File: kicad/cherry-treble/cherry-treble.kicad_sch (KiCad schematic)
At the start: 103 parts

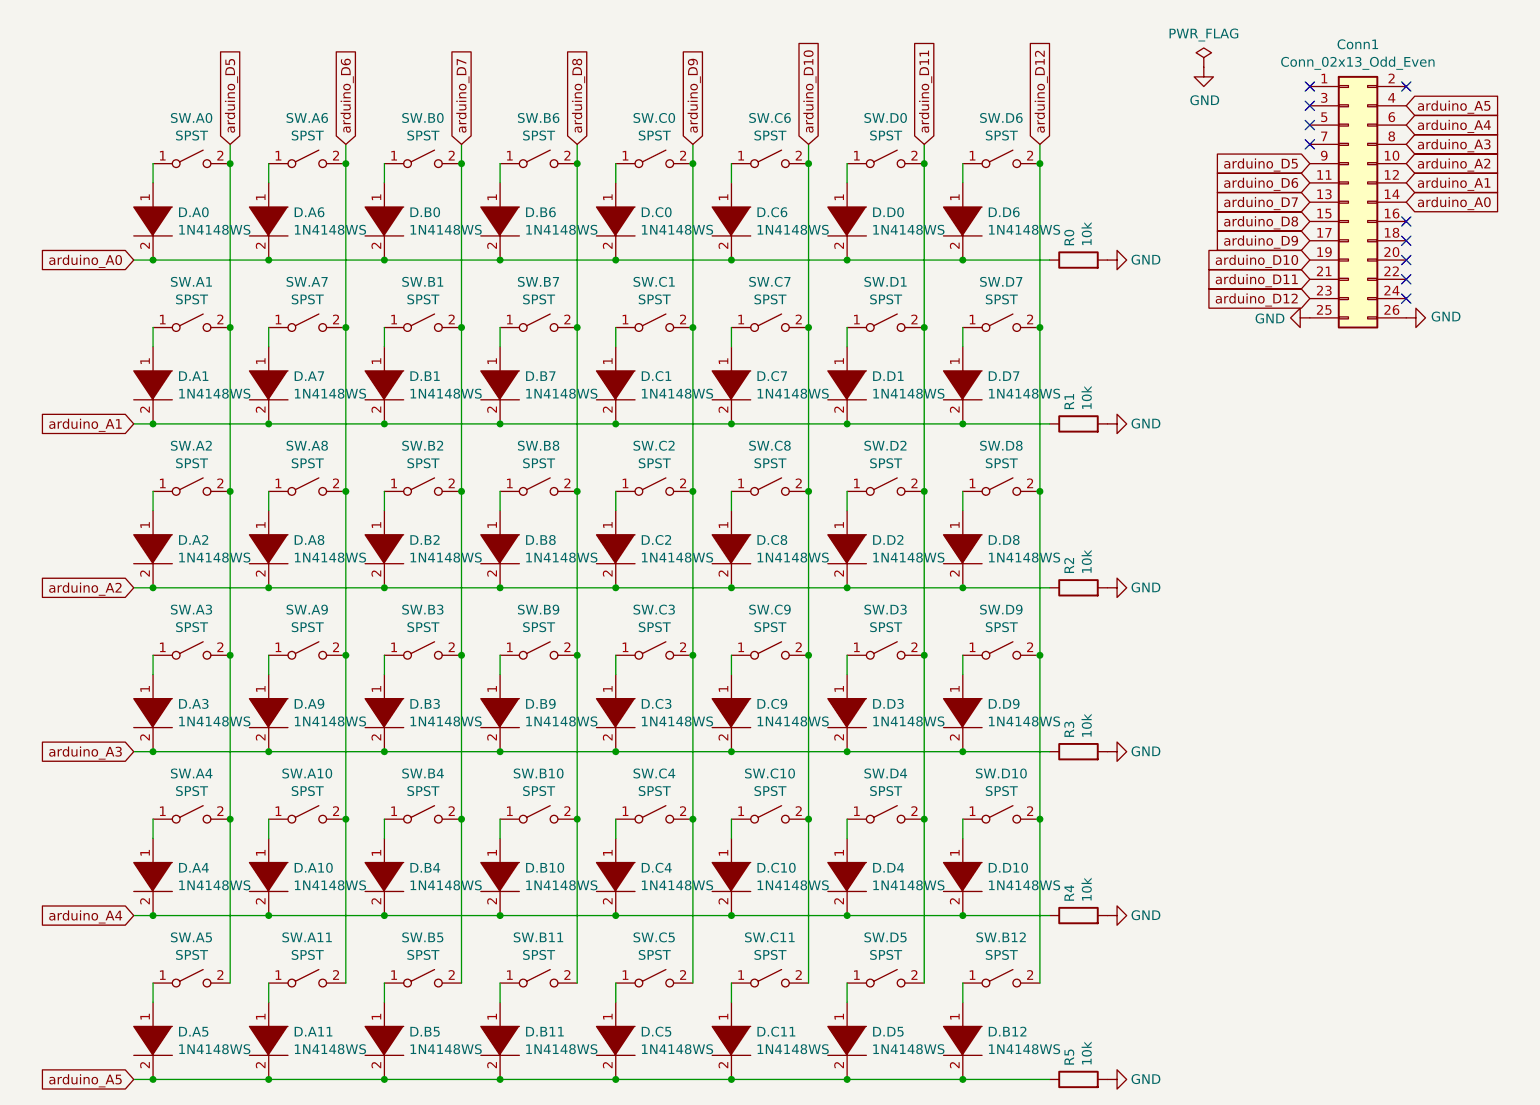
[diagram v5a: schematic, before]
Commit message: Replace diode symbols on cherry treble
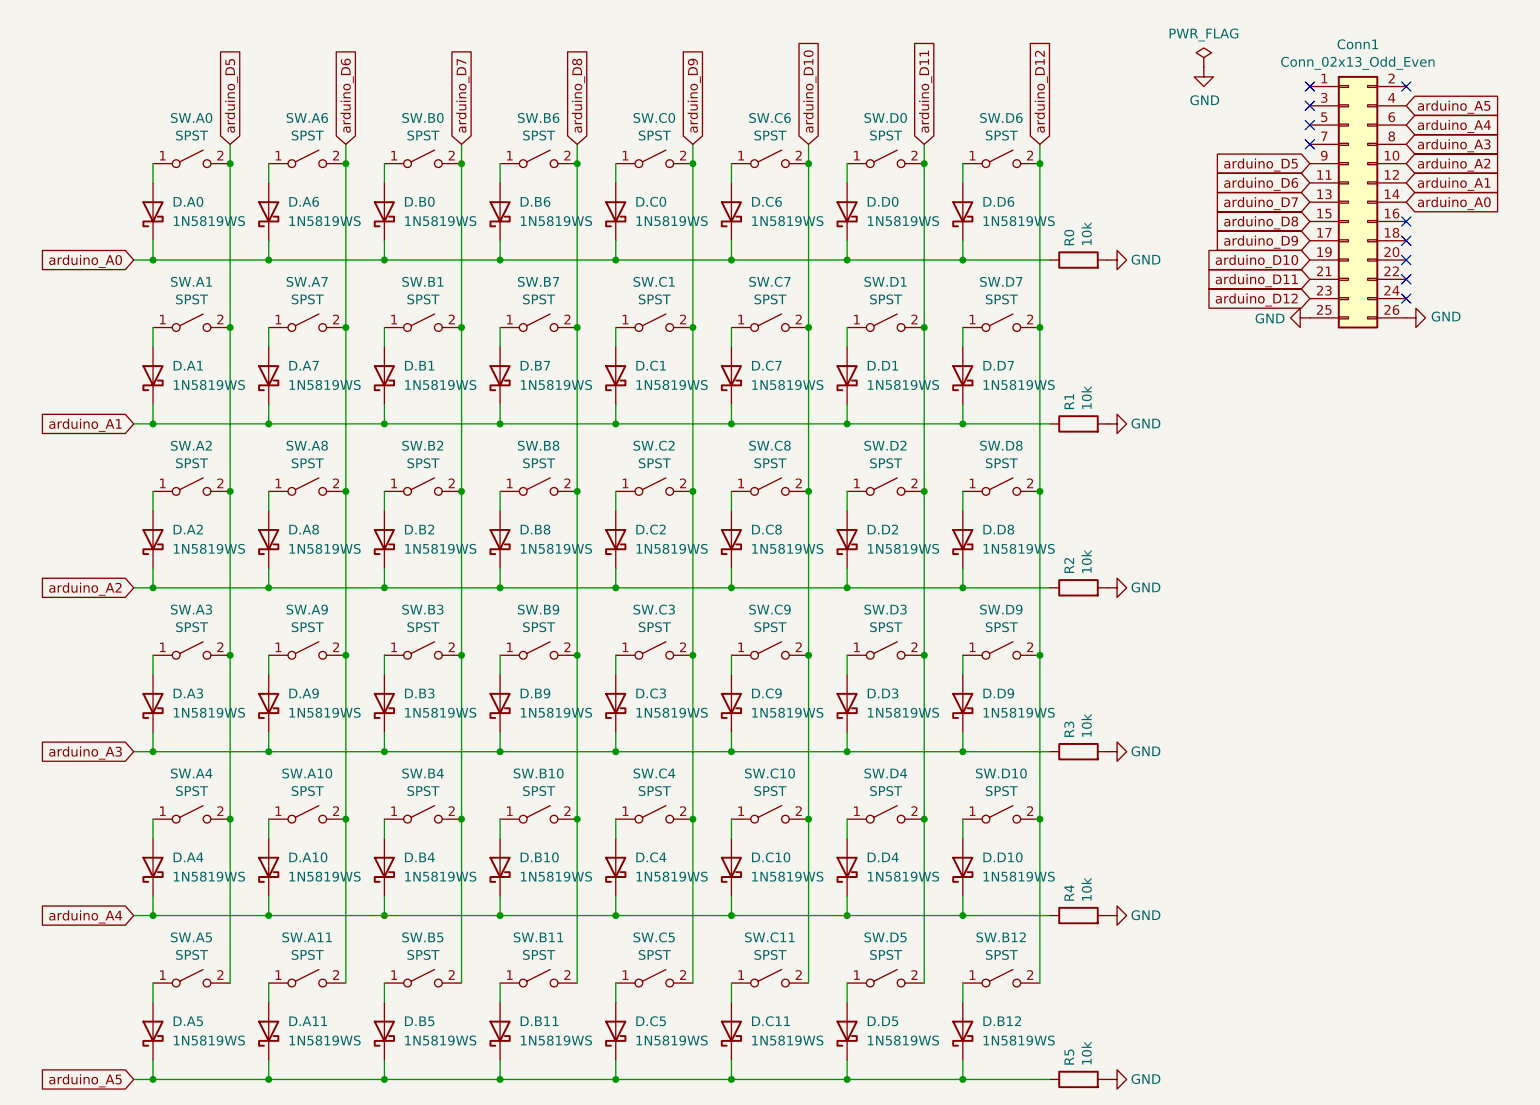
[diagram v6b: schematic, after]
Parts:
- removed D.D6: 1N4148WS, Diode_SMD:D_SOD-323_HandSoldering, symbol pspice:DIODE
- added D.D6: 1N5819WS, Diode_SMD:D_SOD-323_HandSoldering, symbol Diode:1N5819WS
- D.A0, D.A1, D.A10, D.A11, D.A2, D.A3, D.A4, D.A5, D.A6, D.A7, D.A8, D.A9, D.B0, D.B1, D.B10, D.B11, D.B12, D.B2, D.B3, D.B4, D.B5, D.B6, D.B7, D.B8, D.B9, D.C0, D.C1, D.C10, D.C11, D.C2, D.C3, D.C4, D.C5, D.C6, D.C7, D.C8, D.C9, D.D0, D.D1, D.D10, D.D2, D.D3, D.D4, D.D5, D.D7, D.D8, D.D9: value 1N4148WS -> 1N5819WS; symbol pspice:DIODE -> Diode:1N5819WS; LCSC Part # (none) -> C2128
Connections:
- net arduino_A0: now also D.A0.1 (K), D.A6.1 (K), D.B0.1 (K), D.B6.1 (K), D.C0.1 (K), D.C6.1 (K), D.D0.1 (K), D.D6.1 (K); no longer D.A0.2 (A), D.A6.2 (A), D.B0.2 (A), D.B6.2 (A), D.C0.2 (A), D.C6.2 (A), D.D0.2 (A)
- net arduino_A1: now also D.A1.1 (K), D.A7.1 (K), D.B1.1 (K), D.B7.1 (K), D.C1.1 (K), D.C7.1 (K), D.D1.1 (K), D.D7.1 (K); no longer D.A1.2 (A), D.A7.2 (A), D.B1.2 (A), D.B7.2 (A), D.C1.2 (A), D.C7.2 (A), D.D1.2 (A), D.D7.2 (A)
- net arduino_A2: now also D.A2.1 (K), D.A8.1 (K), D.B2.1 (K), D.B8.1 (K), D.C2.1 (K), D.C8.1 (K), D.D2.1 (K), D.D8.1 (K); no longer D.A2.2 (A), D.A8.2 (A), D.B2.2 (A), D.B8.2 (A), D.C2.2 (A), D.C8.2 (A), D.D2.2 (A), D.D8.2 (A)
- net arduino_A3: now also D.A3.1 (K), D.A9.1 (K), D.B3.1 (K), D.B9.1 (K), D.C3.1 (K), D.C9.1 (K), D.D3.1 (K), D.D9.1 (K); no longer D.A3.2 (A), D.A9.2 (A), D.B3.2 (A), D.B9.2 (A), D.C3.2 (A), D.C9.2 (A), D.D3.2 (A), D.D9.2 (A)
- net arduino_A4: now also D.A10.1 (K), D.A4.1 (K), D.B10.1 (K), D.B4.1 (K), D.C10.1 (K), D.C4.1 (K), D.D10.1 (K), D.D4.1 (K); no longer D.A10.2 (A), D.A4.2 (A), D.B10.2 (A), D.B4.2 (A), D.C10.2 (A), D.C4.2 (A), D.D10.2 (A), D.D4.2 (A)
- net arduino_A5: now also D.A11.1 (K), D.A5.1 (K), D.B11.1 (K), D.B12.1 (K), D.B5.1 (K), D.C11.1 (K), D.C5.1 (K), D.D5.1 (K); no longer D.A11.2 (A), D.A5.2 (A), D.B11.2 (A), D.B12.2 (A), D.B5.2 (A), D.C11.2 (A), D.C5.2 (A), D.D5.2 (A)
- net at SW.C4.1 (A): now also D.C4.2 (A); no longer D.C4.1 (K)
- net at SW.C2.1 (A): now also D.C2.2 (A); no longer D.C2.1 (K)
- net at SW.C8.1 (A): now also D.C8.2 (A); no longer D.C8.1 (K)
- net at SW.B4.1 (A): now also D.B4.2 (A); no longer D.B4.1 (K)
- net at SW.D7.1 (A): now also D.D7.2 (A); no longer D.D7.1 (K)
- net at SW.B10.1 (A): now also D.B10.2 (A); no longer D.B10.1 (K)
- net at SW.D6.1 (A): now also D.D6.2 (A)
- net at SW.A6.1 (A): now also D.A6.2 (A); no longer D.A6.1 (K)
- net at SW.A0.1 (A): now also D.A0.2 (A); no longer D.A0.1 (K)
- net at SW.B5.1 (A): now also D.B5.2 (A); no longer D.B5.1 (K)
- net at SW.D1.1 (A): now also D.D1.2 (A); no longer D.D1.1 (K)
- net at SW.D5.1 (A): now also D.D5.2 (A); no longer D.D5.1 (K)
- net at SW.B3.1 (A): now also D.B3.2 (A); no longer D.B3.1 (K)
- net at SW.A5.1 (A): now also D.A5.2 (A); no longer D.A5.1 (K)
- net at SW.A11.1 (A): now also D.A11.2 (A); no longer D.A11.1 (K)
- net at SW.C0.1 (A): now also D.C0.2 (A); no longer D.C0.1 (K)
- net at SW.A4.1 (A): now also D.A4.2 (A); no longer D.A4.1 (K)
- net at SW.D8.1 (A): now also D.D8.2 (A); no longer D.D8.1 (K)
- net at SW.A1.1 (A): now also D.A1.2 (A); no longer D.A1.1 (K)
- net at SW.C11.1 (A): now also D.C11.2 (A); no longer D.C11.1 (K)
- net at SW.C9.1 (A): now also D.C9.2 (A); no longer D.C9.1 (K)
- net at SW.D3.1 (A): now also D.D3.2 (A); no longer D.D3.1 (K)
- net at SW.B2.1 (A): now also D.B2.2 (A); no longer D.B2.1 (K)
- net at SW.A9.1 (A): now also D.A9.2 (A); no longer D.A9.1 (K)
- net at SW.C1.1 (A): now also D.C1.2 (A); no longer D.C1.1 (K)
- net at SW.B9.1 (A): now also D.B9.2 (A); no longer D.B9.1 (K)
- net at SW.B11.1 (A): now also D.B11.2 (A); no longer D.B11.1 (K)
- net at SW.B6.1 (A): now also D.B6.2 (A); no longer D.B6.1 (K)
- net at SW.B1.1 (A): now also D.B1.2 (A); no longer D.B1.1 (K)
- net at SW.B7.1 (A): now also D.B7.2 (A); no longer D.B7.1 (K)
- net at SW.A2.1 (A): now also D.A2.2 (A); no longer D.A2.1 (K)
- net at SW.D10.1 (A): now also D.D10.2 (A); no longer D.D10.1 (K)
- net at SW.A10.1 (A): now also D.A10.2 (A); no longer D.A10.1 (K)
- net at SW.B0.1 (A): now also D.B0.2 (A); no longer D.B0.1 (K)
- net at SW.A3.1 (A): now also D.A3.2 (A); no longer D.A3.1 (K)
- net at SW.D2.1 (A): now also D.D2.2 (A); no longer D.D2.1 (K)
- net at SW.C7.1 (A): now also D.C7.2 (A); no longer D.C7.1 (K)
- net at SW.C3.1 (A): now also D.C3.2 (A); no longer D.C3.1 (K)
- net at SW.A8.1 (A): now also D.A8.2 (A); no longer D.A8.1 (K)
- net at SW.C5.1 (A): now also D.C5.2 (A); no longer D.C5.1 (K)
- net at SW.A7.1 (A): now also D.A7.2 (A); no longer D.A7.1 (K)
- net at SW.B12.1 (A): now also D.B12.2 (A); no longer D.B12.1 (K)
- net at SW.D0.1 (A): now also D.D0.2 (A); no longer D.D0.1 (K)
- net at SW.C10.1 (A): now also D.C10.2 (A); no longer D.C10.1 (K)
- net at SW.B8.1 (A): now also D.B8.2 (A); no longer D.B8.1 (K)
- net at SW.D4.1 (A): now also D.D4.2 (A); no longer D.D4.1 (K)
- net at SW.C6.1 (A): now also D.C6.2 (A); no longer D.C6.1 (K)
- net at SW.D9.1 (A): now also D.D9.2 (A); no longer D.D9.1 (K)
